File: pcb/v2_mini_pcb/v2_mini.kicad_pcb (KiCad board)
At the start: 6 copper layers, 70.8 x 36 mm, 107 parts, among them J1 Conn_Coaxial, J2 GTFP08441BEU, J3 SFV24R-2STE1HLF, J5 TC2030, J6 USB4105-GF-A, Q1 NTNS3164NZT5G, SW1 SW_Push, SW2 SW_Push, SW3 SW_Push, SW4 SW_Push, SW5 SW_Push, SW6 SW_Push, U1 UM980, U10 TPS63802DLAR, U3 SCH16T-K01-1, U4 LP5813ADRRR, U5 TCA9536ADTMR, U6 TPD4EUSB30, U8 BQ25622ERYKR, U9 MAX17048G_T10

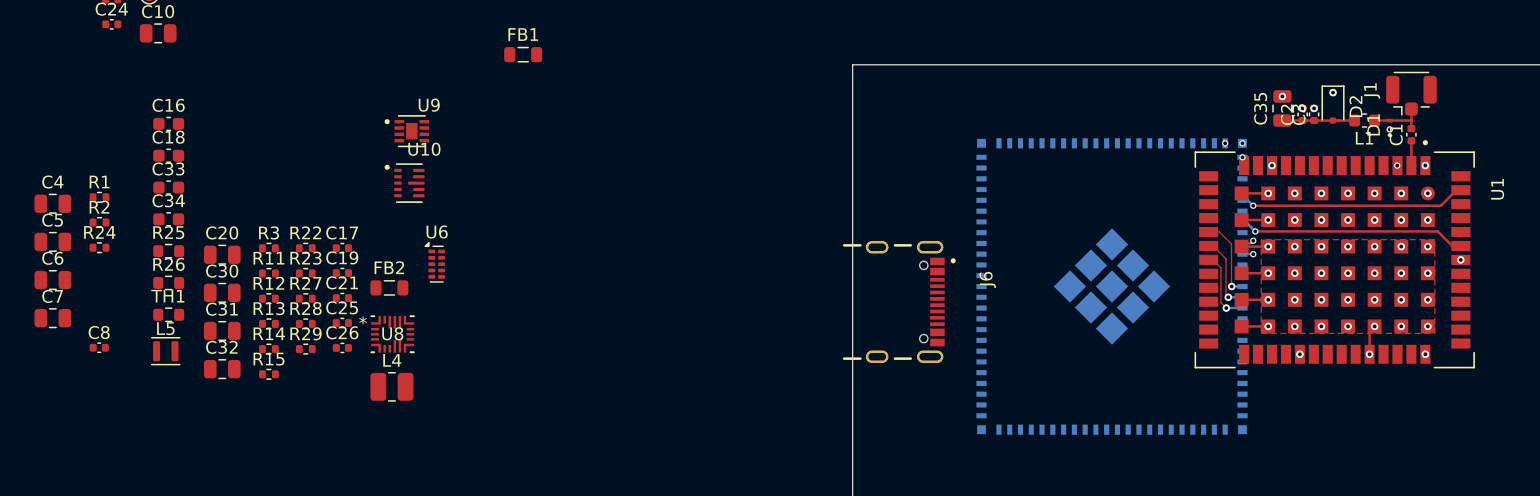
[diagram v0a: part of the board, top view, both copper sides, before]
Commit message: edit gnss pcb
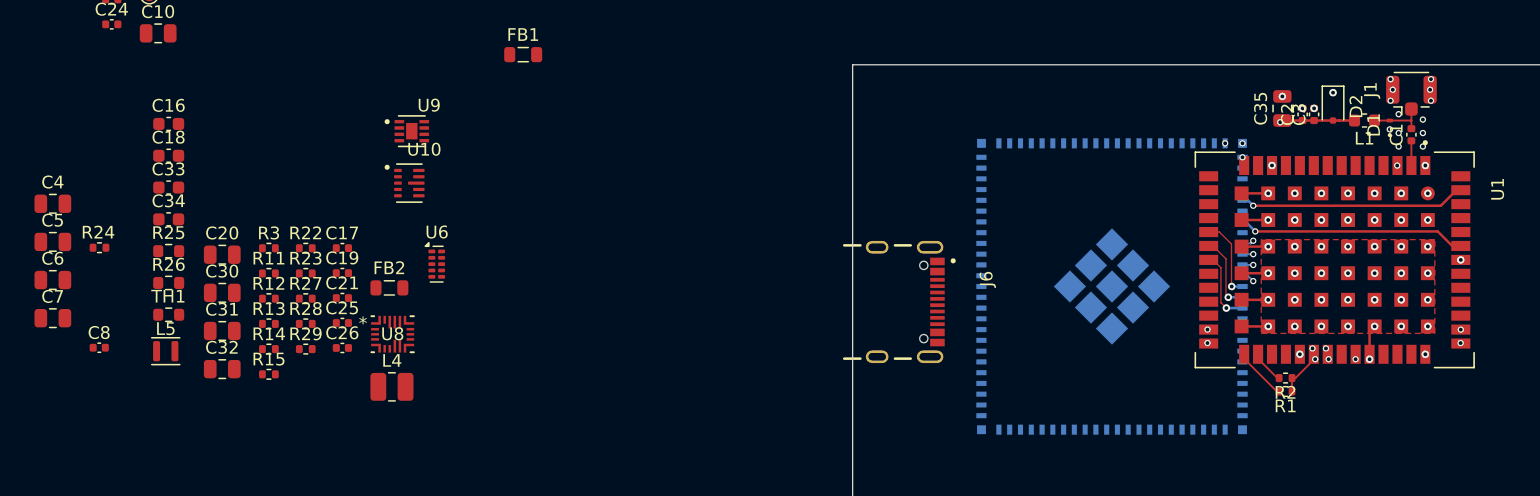
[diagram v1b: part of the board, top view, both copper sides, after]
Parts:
- moved R1 94.9 mm to (111.4, 103.8), turned to 180 degrees
- moved R2 94.4 mm to (111.4, 102.7), turned to 180 degrees
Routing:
- net +3V3_GNSS: track 5.70 -> 31.6 mm, vias 0 -> 6
- net /ESP32-S31 MCU/GNSS_RXD1: track 0.85 -> 22.2 mm, vias 1 -> 2
- net /ESP32-S31 MCU/GNSS_TXD1: track 0.94 -> 20.6 mm, vias 1 -> 2
- net /ESP32-S31 MCU/GNSS_TXD2: track 0.00 -> 8.86 mm, vias 0 -> 2
- net /ESP32-S31 MCU/GNSS_RXD2: track 0.00 -> 6.62 mm, vias 0 -> 2
- net Net-(R1-Pad2): track 0.00 -> 4.18 mm
- net Net-(R2-Pad2): track 0.00 -> 2.64 mm
- net GND: vias 57 -> 69
- added copper zone on In2.Cu, net +3V3_GNSS

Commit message: vbus connection
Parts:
- added R32: 22k, Resistor_SMD:R_0402_1005Metric, F.Cu at (89.1, 94.9)
- added R33: 22k, Resistor_SMD:R_0402_1005Metric, F.Cu at (89.1, 95.9)
- R11, R12: moved to B.Cu
- moved R10 87.6 mm to (100.5, 84.7), turned to -90 degrees
- moved R17 86.7 mm to (101.6, 84.7), turned to -90 degrees
- moved R12 51.0 mm to (82.0, 98.5)
- moved R11 50.9 mm to (82.0, 95.5)
- moved U6 41.4 mm to (85.7, 96.5), turned to 180 degrees
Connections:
- J6 pad A5: /ESP32-S31 MCU/USB_CC1 -> Net-(J6-CC1)
- J6 pad B5: /ESP32-S31 MCU/USB_CC2 -> Net-(J6-CC2)
- R11 pad 2: /ESP32-S31 MCU/USB_CC1 -> Net-(J6-CC1)
- R12 pad 2: /ESP32-S31 MCU/USB_CC2 -> Net-(J6-CC2)
- U6 pad 10: unconnected-(U6-NC-Pad10) -> /ESP32-S31 MCU/USB_DP
- U6 pad 6: unconnected-(U6-NC-Pad6) -> /ESP32-S31 MCU/USB_CC2
- U6 pad 7: unconnected-(U6-NC-Pad7) -> /ESP32-S31 MCU/USB_CC1
- U6 pad 9: unconnected-(U6-NC-Pad9) -> /ESP32-S31 MCU/USB_DN
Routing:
- net /ESP32-S31 MCU/USB_CC2: track 0.00 -> 32.4 mm, vias 0 -> 5
- net /ESP32-S31 MCU/USB_CC1: track 0.00 -> 27.3 mm, vias 0 -> 3
- net /ESP32-S31 MCU/USB_DP: track 0.00 -> 25.1 mm
- net /ESP32-S31 MCU/USB_DN: track 0.00 -> 24.3 mm
- net +3V3_GNSS: track 31.6 -> 28.4 mm
- net GND: vias 69 -> 79
- net Net-(U2-USB_DP): vias 0 -> 1
- net Net-(U2-USB_DM): vias 0 -> 1
- net Net-(J6-VBUS): vias 0 -> 4

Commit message: pcb power done
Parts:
- moved C36 157.3 mm to (127.3, 111.6)
- moved R20 157.3 mm to (130.8, 111.4)
- moved R24 109.3 mm to (127.0, 92.9), turned to -90 degrees
- moved C7 106.6 mm to (120.5, 104.0), turned to 90 degrees
- moved C6 104.8 mm to (118.5, 104.0), turned to 90 degrees
- moved C5 103.1 mm to (116.4, 104.0), turned to 90 degrees
- moved C4 101.4 mm to (114.4, 104.0), turned to 90 degrees
- moved C8 95.2 mm to (112.9, 103.2), turned to 90 degrees
- moved R16 77.7 mm to (85.3, 93.8), turned to 90 degrees
- moved R21 76.2 mm to (86.3, 93.8), turned to -90 degrees
- moved C34 73.6 mm to (96.2, 81.1), turned to -90 degrees
- moved L5 72.3 mm to (92.2, 79.8)
- moved R25 72.2 mm to (94.7, 82.4), turned to -90 degrees
- moved R26 70.6 mm to (93.0, 84.6), turned to 180 degrees
- moved TH1 70.0 mm to (93.1, 101.0)
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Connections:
- J6 pad A5: Net-(J6-CC1) -> /ESP32-S31 MCU/USB_CC1
- J6 pad B5: Net-(J6-CC2) -> /ESP32-S31 MCU/USB_CC2
- R11 pad 2: Net-(J6-CC1) -> /ESP32-S31 MCU/USB_CC1
- R12 pad 2: Net-(J6-CC2) -> /ESP32-S31 MCU/USB_CC2
- R32 pad 1: Net-(J6-CC2) -> /ESP32-S31 MCU/USB_CC2
- R33 pad 1: Net-(J6-CC1) -> /ESP32-S31 MCU/USB_CC1
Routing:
- net /ESP32-S31 MCU/USB_VBUS_S: track 0.00 -> 31.6 mm, vias 0 -> 2
- net /ESP32-S31 MCU/CHG_PG: track 0.00 -> 27.4 mm, vias 0 -> 2
- net /ESP32-S31 MCU/POW_SCL: track 0.00 -> 23.7 mm, vias 0 -> 2
- net /ESP32-S31 MCU/POW_SDA: track 0.00 -> 19.8 mm, vias 0 -> 3
- net /ESP32-S31 MCU/CHG_INT: track 0.00 -> 19.3 mm, vias 0 -> 2
- net +3V3: track 0.00 -> 17.9 mm, vias 0 -> 10
- net /ESP32-S31 MCU/CHG_STAT: track 0.00 -> 16.5 mm, vias 0 -> 2
- net /ESP32-S31 MCU/BAT_ALRT: track 0.00 -> 13.2 mm, vias 0 -> 2
- net +3V3_GNSS: track 28.4 -> 38.4 mm, vias 6 -> 10
- net GND: track 15.0 -> 20.3 mm, vias 79 -> 139
- net /ESP32-S31 MCU/USB_CC1: track 27.3 -> 31.6 mm
- net Net-(U8-REGN): track 0.00 -> 3.88 mm
- net Net-(U10-FB): track 0.00 -> 3.60 mm
- net Net-(U8-BTST): track 0.00 -> 2.70 mm, vias 0 -> 2
- net Net-(U10-L2): track 0.00 -> 1.91 mm
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- added copper zone on F.Cu, net +3V3
- added copper zone on F.Cu, net +3V3_GNSS
- added copper zone on F.Cu, net /Power + USB/3V3_RAW
- added copper zone on F.Cu, net Net-(BT1-+)
- added copper zone on F.Cu, net Net-(J6-VBUS)
- added copper zone on In2.Cu, net Net-(J6-VBUS)
- added copper zone on F.Cu, net Net-(U8-PMID)
- added copper zone on F.Cu, net Net-(U8-SW)
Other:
- outline, holes or cut-outs redrawn

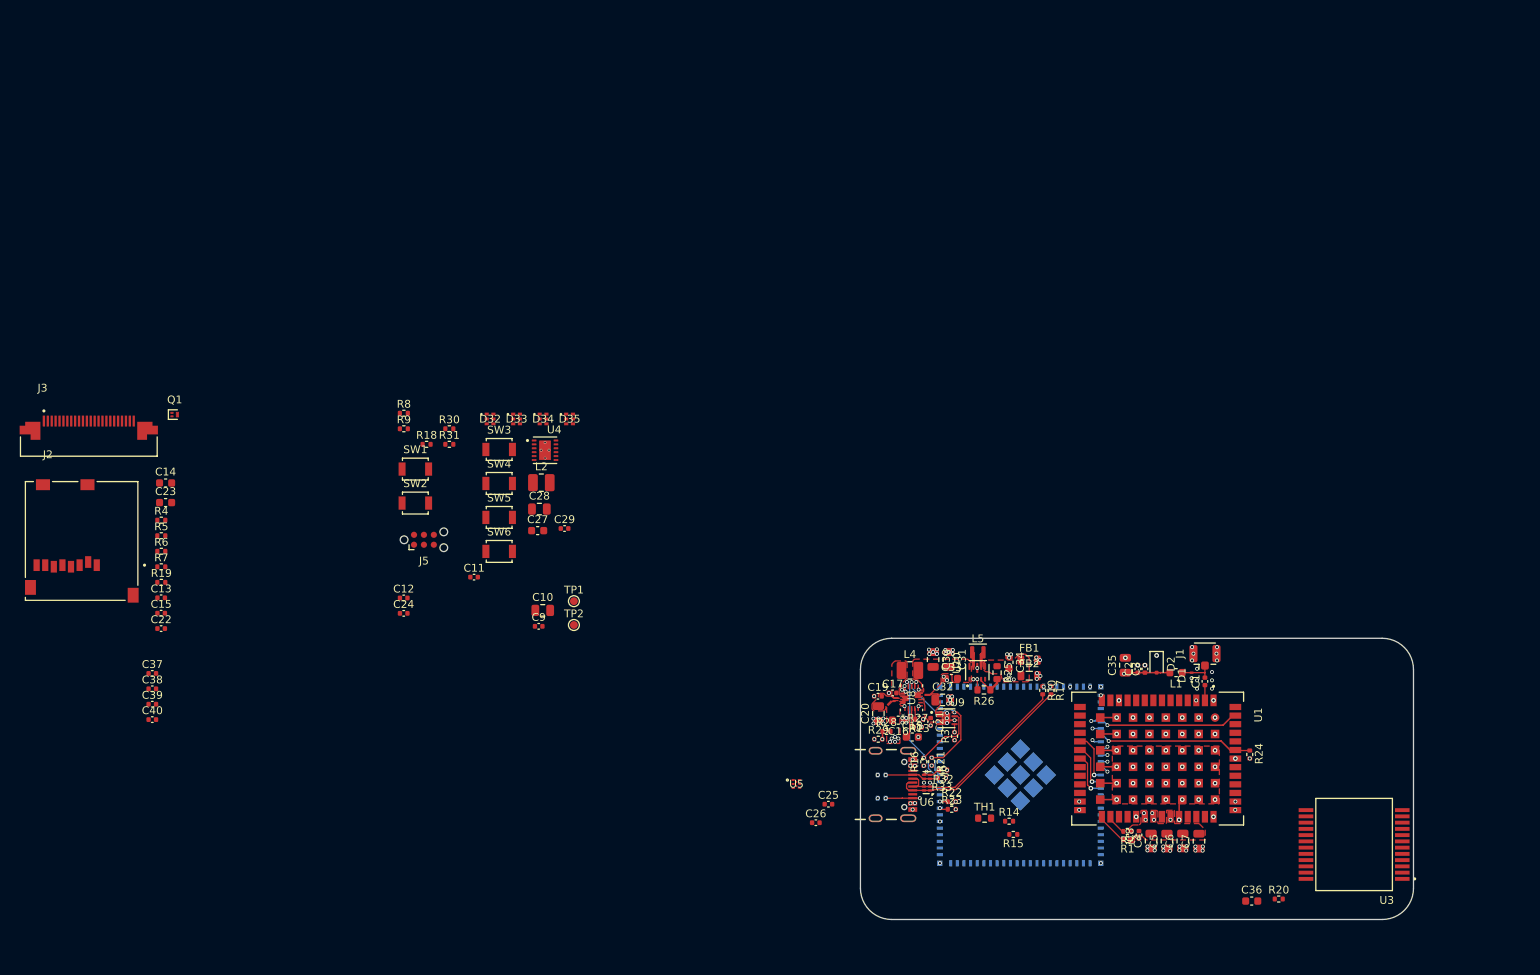
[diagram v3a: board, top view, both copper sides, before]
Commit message: move gnss closer
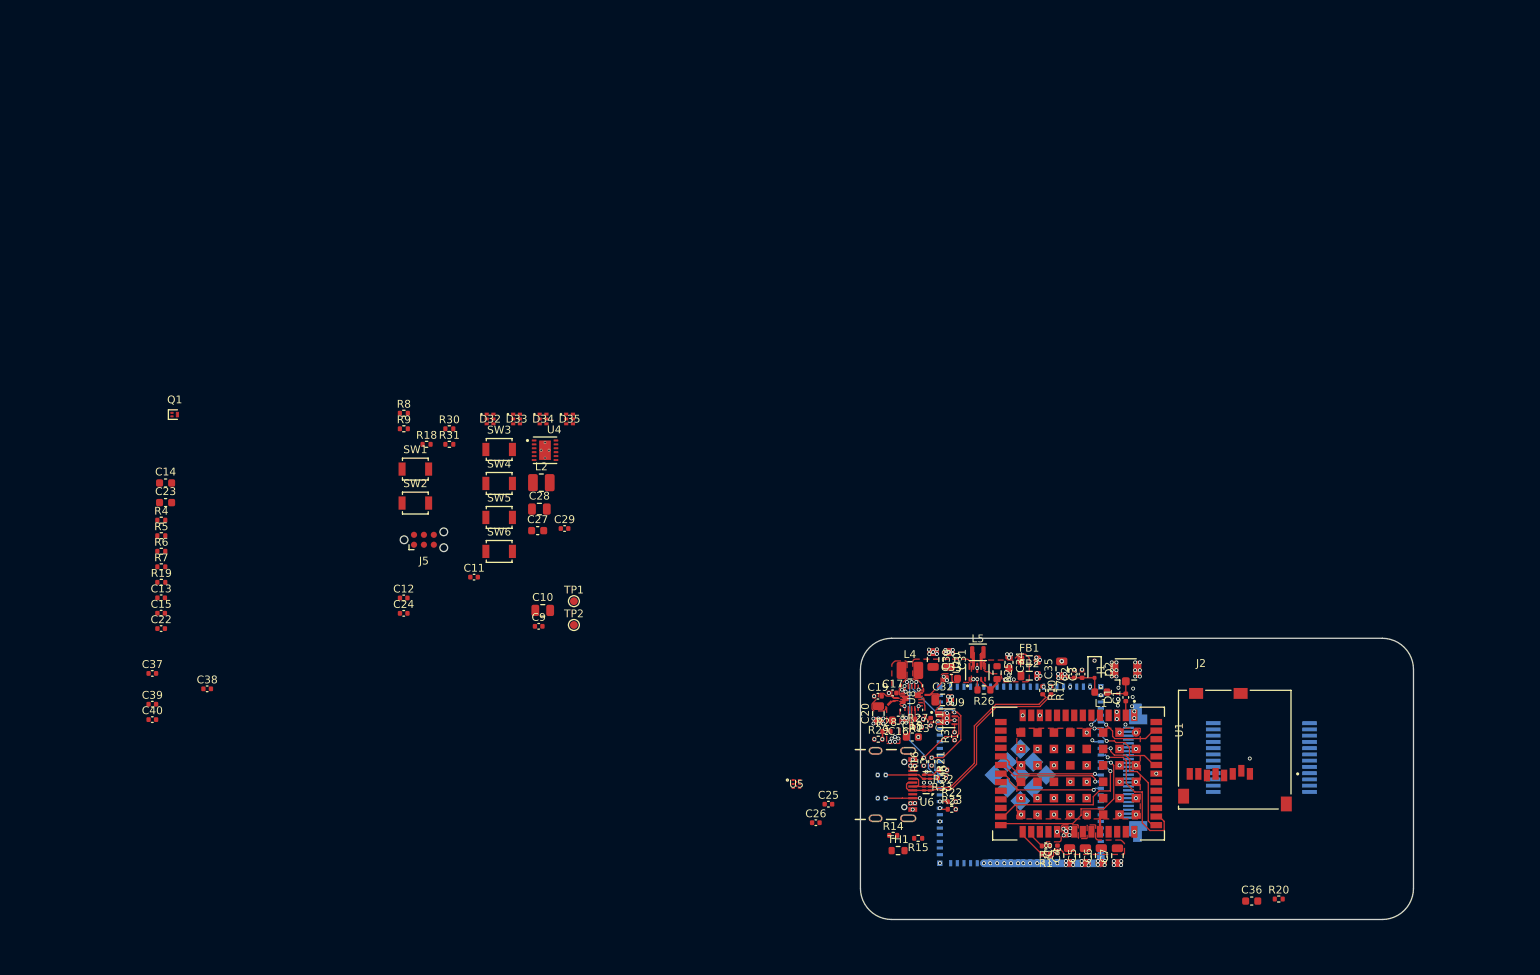
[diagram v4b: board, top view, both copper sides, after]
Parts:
- removed R24: 10k, Resistor_SMD:R_0402_1005Metric
- J3, U3: moved to B.Cu
- moved J2 150.0 mm to (125.1, 98.2)
- moved J3 142.0 mm to (113.9, 95.2), turned to -90 degrees
- moved U3 16.3 mm to (128.5, 93.3)
- moved R14 14.9 mm to (81.4, 103.2)
- moved R15 12.2 mm to (84.6, 103.6)
- moved TH1 11.8 mm to (82.0, 105.2)
- moved C7 10.6 mm to (110.1, 105.8)
- moved C4 10.6 mm to (104.0, 105.8)
- moved C5 10.6 mm to (106.0, 105.8)
- moved C6 10.6 mm to (108.0, 105.8)
- moved C8 10.6 mm to (102.4, 105.0)
- moved R1 10.6 mm to (100.9, 105.6)
- moved R2 10.6 mm to (100.9, 104.6)
- moved C1 10.3 mm to (111.2, 85.6)
- moved J1 10.3 mm to (111.2, 82.0)
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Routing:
- net +3V3: track 17.9 -> 35.6 mm
- net /ESP32-S31 MCU/GNSS_TXD2: track 8.86 -> 22.5 mm, vias 2 -> 1
- net /ESP32-S31 MCU/GNSS_RXD2: track 6.62 -> 19.9 mm, vias 2 -> 1
- net /ESP32-S31 MCU/GNSS_RESETN: track 19.9 -> 9.55 mm
- net /ESP32-S31 MCU/GNSS_PPS: track 17.9 -> 8.85 mm
- net /ESP32-S31 MCU/GNSS_ERR: track 5.86 -> 13.9 mm
- net /ESP32-S31 MCU/GNSS_RTK: track 6.02 -> 13.9 mm
- net /ESP32-S31 MCU/GNSS_PVT: track 6.40 -> 14.0 mm
- net +3V3_GNSS: track 38.4 -> 31.2 mm, vias 10 -> 12
- net /ESP32-S31 MCU/GNSS_TXD1: track 20.6 -> 15.2 mm, vias 2 -> 1
- net /ESP32-S31 MCU/GNSS_RXD1: track 22.2 -> 18.6 mm, vias 2 -> 1
- net GND: track 20.3 -> 23.8 mm, vias 139 -> 149
- net /ESP32-S31 MCU/USB_DN: track 24.3 -> 27.5 mm
- net /ESP32-S31 MCU/USB_DP: track 25.1 -> 28.0 mm
- net /ESP32-S31 MCU/CHG_PG: track 27.4 -> 28.7 mm
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- removed copper zone on In2.Cu, net +3V3_GNSS

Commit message: done with lcd pcb
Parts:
- added R24: 10k, Resistor_SMD:R_0402_1005Metric, F.Cu at (0.95, 0.49)
- C15, C22, C23, Q1, R4, R5, R6, R7: moved to B.Cu
- moved Q1 137.1 mm to (114.2, 106.0), turned to 90 degrees
- moved R4 135.0 mm to (115.8, 105.7)
- moved R5 131.9 mm to (113.1, 105.7), turned to 90 degrees
- moved C23 127.5 mm to (112.1, 90.9)
- moved R7 126.2 mm to (111.2, 94.6), turned to 90 degrees
- moved C15 125.8 mm to (112.2, 93.1)
- moved R6 125.6 mm to (110.2, 94.6), turned to 90 degrees
- moved C22 125.4 mm to (112.2, 92.1)
- moved J2 12.4 mm to (127.9, 86.1), turned to 180 degrees
- moved J3 3.23 mm to (117.0, 96.0)
- moved U3 0.82 mm to (127.8, 93.6), turned to -90 degrees
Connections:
- Q1 pad 1: (no net) -> /ESP32-S31 MCU/LCD_BACK
- Q1 pad 2: (no net) -> GND
- Q1 pad 3: (no net) -> Net-(Q1-D)
- R4 pad 1: Net-(Q1-PadD) -> Net-(Q1-D)
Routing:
- net /ESP32-S31 MCU/LCD_CSN: track 0.00 -> 35.3 mm, vias 0 -> 2
- net /ESP32-S31 MCU/LCD_BACK: track 0.00 -> 32.7 mm
- net /ESP32-S31 MCU/LCD_DC: track 0.00 -> 31.2 mm, vias 0 -> 2
- net /ESP32-S31 MCU/LCD_SCLK: track 0.00 -> 31.1 mm, vias 0 -> 2
- net /ESP32-S31 MCU/LCD_SDA: track 0.00 -> 30.7 mm, vias 0 -> 2
- net /ESP32-S31 MCU/LCD_RN: track 0.00 -> 30.5 mm, vias 0 -> 2
- net /ESP32-S31 MCU/LCD_TE: track 0.00 -> 29.1 mm
- net GND: track 23.8 -> 47.1 mm, vias 149 -> 155
- net Net-(J3-Pad2): track 0.00 -> 16.8 mm
- net +3V3: track 35.6 -> 46.0 mm, vias 10 -> 12
- net /ESP32-S31 MCU/USB_VBUS_S: track 31.6 -> 28.2 mm, vias 2 -> 3
- net /ESP32-S31 MCU/USB_CC1: track 31.2 -> 34.4 mm
- net /ESP32-S31 MCU/USB_CC2: track 33.9 -> 32.5 mm
- net /ESP32-S31 MCU/CHG_PG: track 28.7 -> 27.5 mm, vias 2 -> 1
- net Net-(Q1-D): track 0.00 -> 1.05 mm
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
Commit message: imu done
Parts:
- C36, C37, C38, C39, C40, D32, D33, D34, D35, L2, R20, R24, SW1, SW2, SW3, SW4, SW5, SW6, U4: moved to B.Cu
- moved C37 148.0 mm to (133.5, 100.1)
- moved C40 144.2 mm to (130.2, 100.1)
- moved C39 144.1 mm to (130.6, 83.4)
- moved R24 140.9 mm to (109.3, 90.6), turned to 90 degrees
- moved J5 139.7 mm to (159.2, 87.9)
- moved C38 137.0 mm to (130.6, 84.4)
- moved SW3 117.4 mm to (133.9, 110.1), turned to 90 degrees
- moved SW4 110.2 mm to (128.1, 110.1), turned to 90 degrees
- moved D32 108.7 mm to (133.7, 81.8), turned to 180 degrees
- moved C28 106.1 mm to (132.8, 105.0)
- moved L2 102.9 mm to (127.8, 105.2), turned to 180 degrees
- moved SW5 102.9 mm to (122.1, 110.1), turned to 90 degrees
- moved U4 100.4 mm to (123.1, 105.2), turned to 180 degrees
- moved D33 99.7 mm to (127.7, 81.7), turned to 180 degrees
- moved SW6 95.6 mm to (116.2, 110.1), turned to 90 degrees
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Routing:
- net /ESP32-S31 MCU/IMU_RESET_N: track 0.00 -> 59.5 mm, vias 1 -> 2
- net /ESP32-S31 MCU/IMU_MISO: track 0.00 -> 46.1 mm, vias 1 -> 2
- net /ESP32-S31 MCU/IMU_DRDY: track 0.00 -> 45.0 mm, vias 1 -> 2
- net /ESP32-S31 MCU/IMU_SCLK: track 0.00 -> 43.9 mm, vias 1 -> 2
- net /ESP32-S31 MCU/IMU_CS_N: track 0.00 -> 42.4 mm, vias 1 -> 2
- net /ESP32-S31 MCU/IMU_MOSI: track 0.00 -> 41.9 mm, vias 1 -> 2
- net +3V3_GNSS: track 31.2 -> 42.0 mm
- net +3V3_IMU: track 0.00 -> 9.81 mm, vias 3 -> 7
- net Net-(U3-VREGA): track 0.00 -> 4.42 mm
- net Net-(U3-VREGD): track 0.00 -> 3.71 mm
- net /ESP32-S31 MCU/USB_CC1: track 34.4 -> 35.7 mm
- net GND: vias 155 -> 170
